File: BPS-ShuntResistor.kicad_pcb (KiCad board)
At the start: 2 copper layers, 40.1 x 35.1 mm, 11 parts, among them J3 Amp_Conn

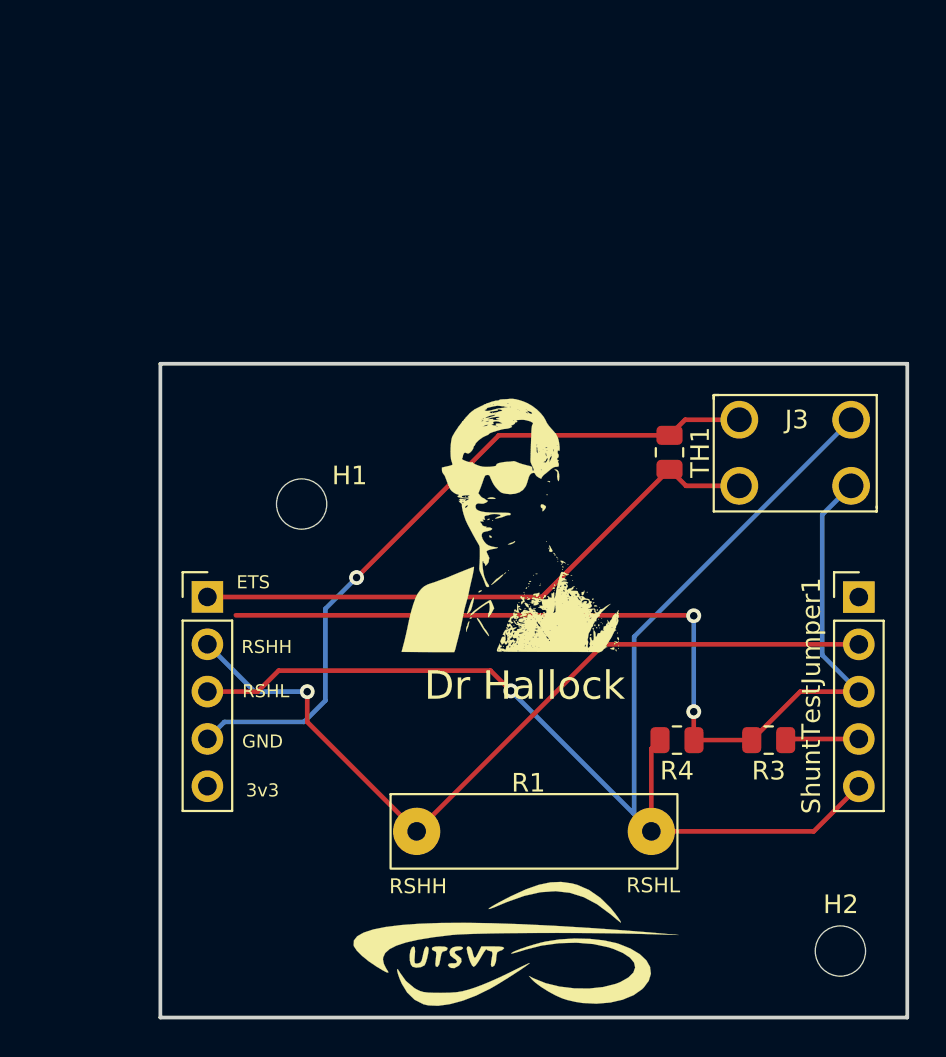
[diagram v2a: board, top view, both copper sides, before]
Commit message: rounding corners, making board a bit smaller
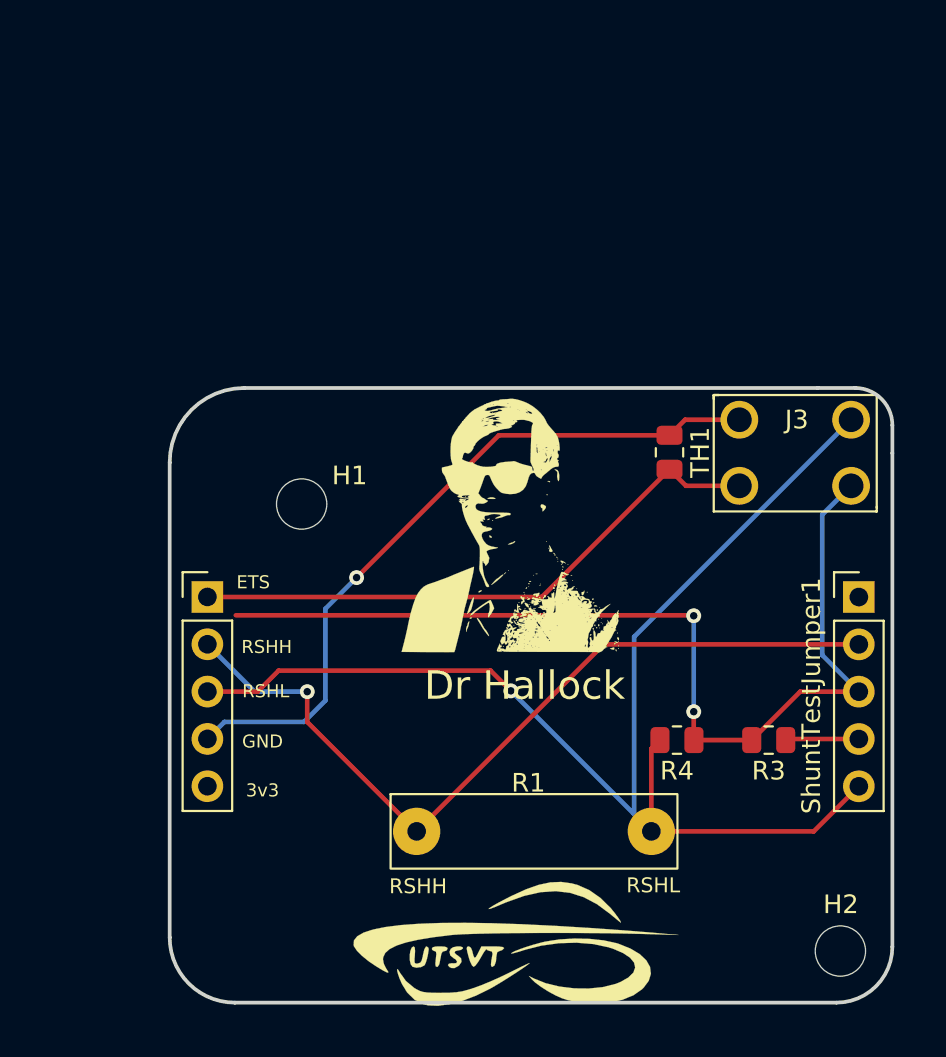
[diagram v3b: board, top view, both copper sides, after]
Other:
- board size 40.1 x 35.1 mm -> 38.8 x 33 mm
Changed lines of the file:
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@@
       (net 3 "RSHL") (pintype "passive"))
   )
-  (gr_rect (start 115 94.9) (end 155.1 130) (layer "Edge.Cuts") (width 0.2) (fill none))
+  (gr_line (start 154.3 126.2) (end 154.300469 99.69887) (layer "Edge.Cuts") (width 0.2))
+  (gr_line (start 119 129.2) (end 151.3 129.2) (layer "Edge.Cuts") (width 0.2))
+  (gr_line (start 154.3 98.2) (end 154.300469 99.69887) (layer "Edge.Cuts") (width 0.2))
+  (gr_line (start 115.5 100.2) (end 115.5 125.7) (layer "Edge.Cuts") (width 0.2))
+  (gr_arc (start 119 129.2) (mid 116.525126 128.174874) (end 115.5 125.7) (layer "Edge.Cuts") (width 0.2))
+  (gr_line (start 152.3 96.2) (end 150.3 96.2) (layer "Edge.Cuts") (width 0.2))
+  (gr_arc (start 115.5 100.2) (mid 116.671573 97.371573) (end 119.5 96.2) (layer "Edge.Cuts") (width 0.2))
+  (gr_arc (start 154.3 126.2) (mid 153.42132 128.32132) (end 151.3 129.2) (layer "Edge.Cuts") (width 0.2))
+  (gr_arc (start 152.3 96.2) (mid 153.714214 96.785786) (end 154.3 98.2) (layer "Edge.Cuts") (width 0.2))
+  (gr_line (start 150.3 96.2) (end 119.5 96.2) (layer "Edge.Cuts") (width 0.2))
   (gr_text "RSHL" (at 141.46 122.905) (layer "F.SilkS")
     (effects (font (size 0.8 0.8) (thickness 0.2)))
@@
     (effects (font (size 1.5 1.5) (thickness 0.3)))
   )
-  (dimension (type aligned) (layer "Cmts.User")
-    (pts (xy 155.075 94.32) (xy 114.975 94.32))
-    (height 4.87)
-    (gr_text "40.1000 mm" (at 135.025 87.65) (layer "Cmts.User")
-      (effects (font (size 1.5 1.5) (thickness 0.3)))
-    )
-    (format (units 3) (units_format 1) (precision 4))
-    (style (thickness 0.2) (arrow_length 1.27) (text_position_mode 0) (extension_height 0.58642) (extension_offset 0.5) keep_text_aligned)
-  )
-  (dimension (type aligned) (layer "Cmts.User")
-    (pts (xy 114.265 94.9) (xy 114.265 130))
-    (height 3.49)
-    (gr_text "35.1000 mm" (at 108.975 112.45 90) (layer "Cmts.User")
-      (effects (font (size 1.5 1.5) (thickness 0.3)))
-    )
-    (format (units 3) (units_format 1) (precision 4))
-    (style (thickness 0.2) (arrow_length 1.27) (text_position_mode 0) (extension_height 0.58642) (extension_offset 0.5) keep_text_aligned)
-  )
-  (dimension (type aligned) (layer "Cmts.User")
-    (pts (xy 151.51 126.405) (xy 151.51 130.005))
-    (height -3.6)
-    (gr_text "3.6000 mm" (at 156.585 128.105 90) (layer "Cmts.User")
-      (effects (font (size 0.5 0.5) (thickness 0.3)))
-    )
-    (format (units 3) (units_format 1) (precision 4))
-    (style (thickness 0.2) (arrow_length 1.27) (text_position_mode 2) (extension_height 0.58642) (extension_offset 0.5) keep_text_aligned)
-  )
-  (dimension (type aligned) (layer "Cmts.User")
-    (pts (xy 122.585 102.43) (xy 122.585 94.83))
-    (height -7.625)
-    (gr_text "7.6000 mm" (at 114.335 98.63 90) (layer "Cmts.User")
-      (effects (font (size 0.5 0.5) (thickness 0.3)))
-    )
-    (format (units 3) (units_format 1) (precision 4))
-    (style (thickness 0.2) (arrow_length 1.27) (text_position_mode 0) (extension_height 0.58642) (extension_offset 0.5) keep_text_aligned)
-  )
-  (dimension (type aligned) (layer "Cmts.User")
-    (pts (xy 154.625 97.925) (xy 154.625 94.925))
-    (height 4.225)
-    (gr_text "3.0000 mm" (at 160.25 96.5 90) (layer "Cmts.User")
-      (effects (font (size 0.6 0.6) (thickness 0.3)))
-    )
-    (format (units 3) (units_format 1) (precision 4))
-    (style (thickness 0.2) (arrow_length 1.27) (text_position_mode 2) (extension_height 0.58642) (extension_offset 0.5) keep_text_aligned)
-  )
-  (dimension (type aligned) (layer "Cmts.User")
-    (pts (xy 128.76 120.005) (xy 128.76 130.005))
-    (height 13.85)
-    (gr_text "10.0000 mm" (at 114.16 125.005 90) (layer "Cmts.User")
-      (effects (font (size 0.6 0.6) (thickness 0.3)))
-    )
-    (format (units 3) (units_format 1) (precision 4))
-    (style (thickness 0.2) (arrow_length 1.27) (text_position_mode 0) (extension_height 0.58642) (extension_offset 0.5) keep_text_aligned)
-  )
-  (dimension (type aligned) (layer "Cmts.User")
-    (pts (xy 128.76 120.005) (xy 115.01 120.005))
-    (height -10.025)
-    (gr_text "13.7500 mm" (at 121.735 130.93) (layer "Cmts.User")
-      (effects (font (size 0.6 0.6) (thickness 0.3)))
-    )
-    (format (units 3) (units_format 1) (precision 4))
-    (style (thickness 0.2) (arrow_length 1.27) (text_position_mode 2) (extension_height 0.58642) (extension_offset 0.5) keep_text_aligned)
-  )
-  (dimension (type aligned) (layer "Cmts.User")
-    (pts (xy 151.51 126.405) (xy 155.11 126.405))
-    (height 3.65)
-    (gr_text "3.6000 mm" (at 153.41 131.38) (layer "Cmts.User")
-      (effects (font (size 0.5 0.5) (thickness 0.3)))
-    )
-    (format (units 3) (units_format 1) (precision 4))
-    (style (thickness 0.2) (arrow_length 1.27) (text_position_mode 2) (extension_height 0.58642) (extension_offset 0.5) keep_text_aligned)
-  )
-  (dimension (type aligned) (layer "Cmts.User")
-    (pts (xy 122.585 102.505) (xy 114.985 102.505))
-    (height 7.675)
-    (gr_text "7.6000 mm" (at 118.785 94.205) (layer "Cmts.User")
-      (effects (font (size 0.5 0.5) (thickness 0.3)))
-    )
-    (format (units 3) (units_format 1) (precision 4))
-    (style (thickness 0.2) (arrow_length 1.27) (text_position_mode 0) (extension_height 0.58642) (extension_offset 0.5) keep_text_aligned)
-  )
-  (dimension (type aligned) (layer "Cmts.User")
-    (pts (xy 152.085 97.905) (xy 155.085 97.905))
-    (height -3.35)
-    (gr_text "3.0000 mm" (at 153.51 93.38) (layer "Cmts.User")
-      (effects (font (size 0.6 0.6) (thickness 0.3)))
-    )
-    (format (units 3) (units_format 1) (precision 4))
-    (style (thickness 0.2) (arrow_length 1.27) (text_position_mode 2) (extension_height 0.58642) (extension_offset 0.5) keep_text_aligned)
-  )
   (segment (start 146.085 101.453) (end 143.2205 101.453) (width 0.25) (layer "F.Cu") (net 1))

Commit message: fixing pcb to look nicer
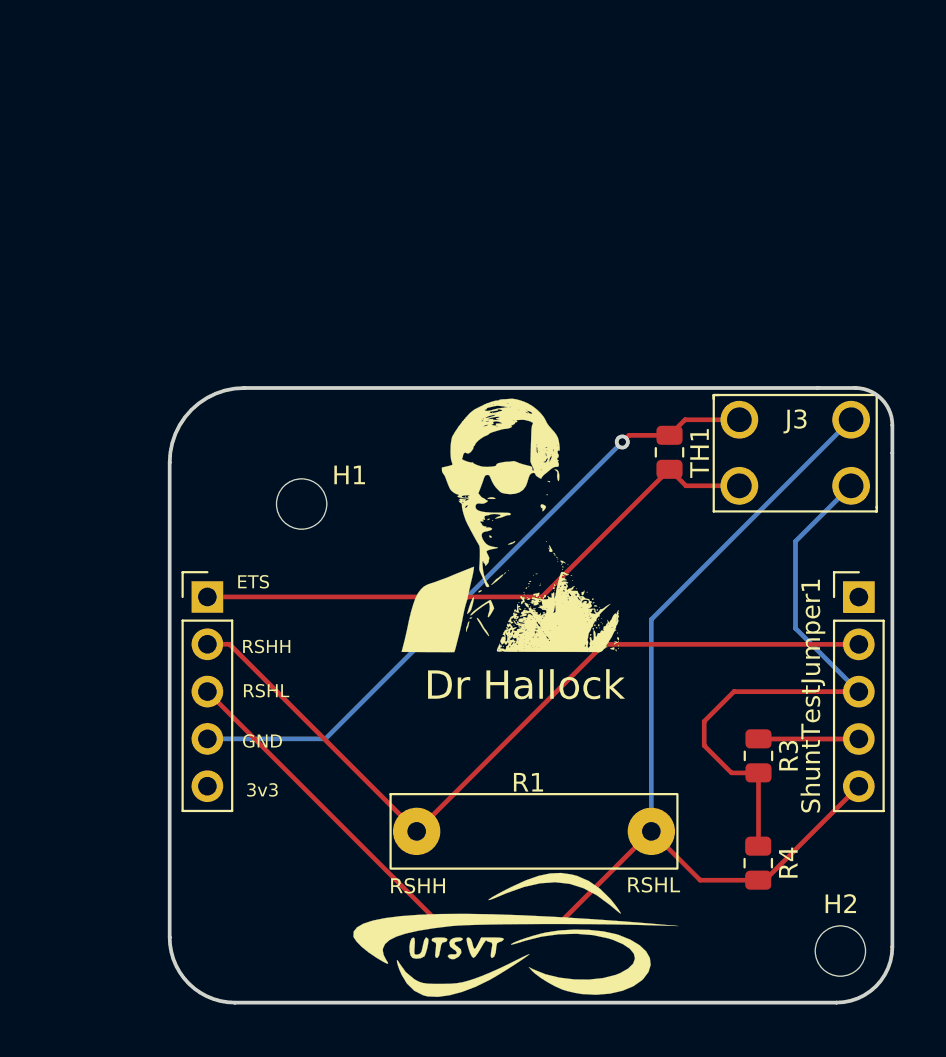
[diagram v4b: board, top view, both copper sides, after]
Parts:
- moved R4 7.92 mm to (147.1, 121.7), turned to -90 degrees
- moved R3 1.01 mm to (147.1, 116.0), turned to -90 degrees
- moved LOGO1 0.48 mm to (133.8, 125.7)
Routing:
- net Net-(J3-Pad2): track 53.7 -> 31.4 mm, vias 2 -> 0
- net GND: track 38.6 -> 35.7 mm
- net /TestIn: track 4.24 -> 5.39 mm
- net RSHH: track 44.2 -> 43.3 mm, vias 1 -> 0
- net RSHL: track 72.4 -> 71.8 mm, vias 1 -> 0

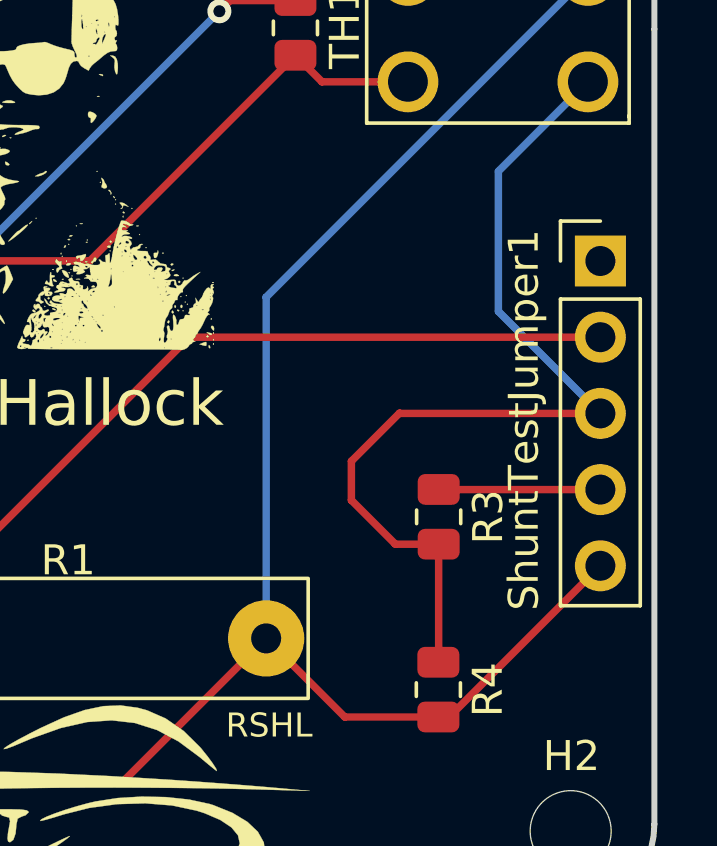
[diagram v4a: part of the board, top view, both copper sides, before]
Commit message: resistor placement change
make tracks more readable + add some text for pins
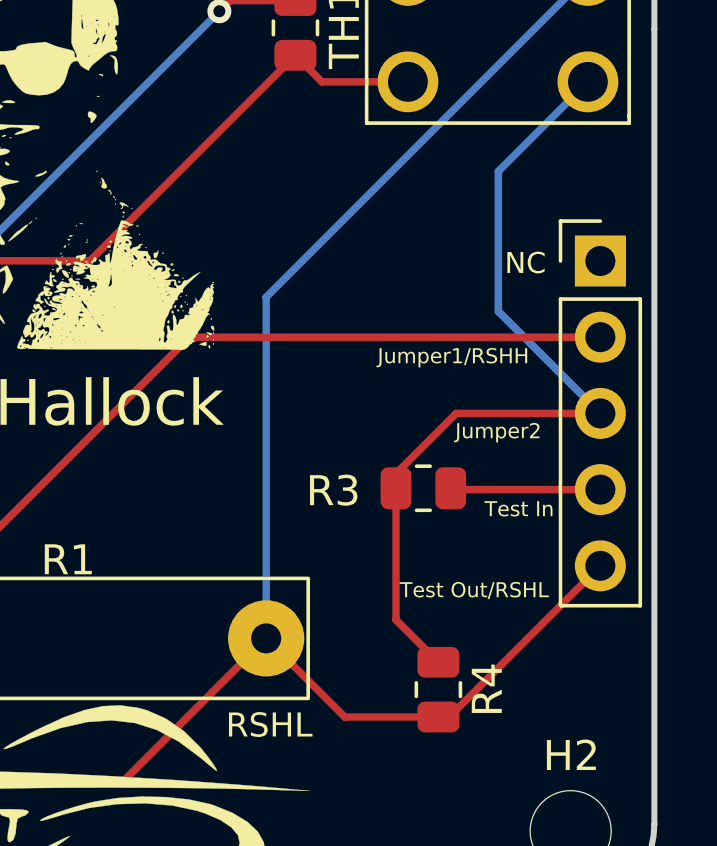
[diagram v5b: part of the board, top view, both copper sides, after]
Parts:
- moved R3 1.08 mm to (146.6, 115.0), turned to 180 degrees
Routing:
- net Net-(J3-Pad2): track 31.4 -> 28.2 mm
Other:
- board text added: "Jumper1/RSHH"
- board text added: "Jumper2"
- board text added: "NC"
- board text added: "Test In"
- board text added: "Test Out/RSHL"
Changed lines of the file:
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@@
   )
   (footprint "Resistor_SMD:R_0805_2012Metric" (layer "F.Cu")
-    (at 147.11 115.9525 -90)
+    (at 146.6 115 180)
     (descr "Resistor SMD 0805 (2012 Metric), square (rectangular) end terminal, IPC_7351 nominal, (Body size source: IPC-SM-782 page 72, https://www.pcb-3d.com/wordpress/wp-content/uploads/ipc-sm-782a_amendment_1_and_2.pdf), generated with kicad-footprint-generator")
     (tags "resistor")
@@
     (property "Sheetname" "")
     (attr smd)
-    (fp_text reference "R3" (at 0 -1.65 -270) (layer "F.SilkS")
+    (fp_text reference "R3" (at 3 -0.1) (layer "F.SilkS")
       (effects (font (size 1 1) (thickness 0.15)))
     )
-    (fp_text value "34k" (at 0 1.65 -270) (layer "F.Fab")
+    (fp_text value "34k" (at 0 1.65) (layer "F.Fab")
       (effects (font (size 1 1) (thickness 0.15)))
     )
-    (fp_text user "${REFERENCE}" (at 0 0 -270) (layer "F.Fab")
+    (fp_text user "${REFERENCE}" (at 0 0) (layer "F.Fab")
       (effects (font (size 0.5 0.5) (thickness 0.08)))
     )
@@
     (fp_line (start 1 0.625) (end -1 0.625) (layer "F.Fab") (width 0.1))
     (fp_line (start -1 0.625) (end -1 -0.625) (layer "F.Fab") (width 0.1))
-    (pad "1" smd roundrect (at -0.9125 0 270) (size 1.025 1.4) (layers "F.Cu" "F.Paste" "F.Mask") (roundrect_rratio 0.243902439)
+    (pad "1" smd roundrect (at -0.9125 0 180) (size 1.025 1.4) (layers "F.Cu" "F.Paste" "F.Mask") (roundrect_rratio 0.243902439)
       (net 6 "/TestIn") (pintype "passive"))
-    (pad "2" smd roundrect (at 0.9125 0 270) (size 1.025 1.4) (layers "F.Cu" "F.Paste" "F.Mask") (roundrect_rratio 0.243902439)
+    (pad "2" smd roundrect (at 0.9125 0 180) (size 1.025 1.4) (layers "F.Cu" "F.Paste" "F.Mask") (roundrect_rratio 0.243902439)
       (net 7 "Net-(J3-Pad2)") (pintype "passive"))
     (model "${KICAD6_3DMODEL_DIR}/Resistor_SMD.3dshapes/R_0805_2012Metric.wrl"
@@
     (property "Sheetname" "")
     (attr through_hole)
-    (fp_text reference "ShuntTestJumper1" (at -2.55 5.3 90) (layer "F.SilkS")
+    (fp_text reference "ShuntTestJumper1" (at -2.55 5.3 90) (layer "F.SilkS") hide
       (effects (font (size 1 1) (thickness 0.15)))
     )
@@
     (effects (font (size 0.7 0.7) (thickness 0.175)))
   )
+  (gr_text "Jumper1/RSHH\n" (at 147.6 110.6) (layer "F.SilkS")
+    (effects (font (size 0.5 0.5) (thickness 0.125)))
+  )
   (gr_text "ETS" (at 119.985 106.63) (layer "F.SilkS")
     (effects (font (size 0.7 0.7) (thickness 0.175)))
@@
     (effects (font (size 0.7 0.7) (thickness 0.175)))
   )
+  (gr_text "Jumper2" (at 149.1 113.1) (layer "F.SilkS")
+    (effects (font (size 0.5 0.5) (thickness 0.125)))
+  )
+  (gr_text "NC\n" (at 150 107.5) (layer "F.SilkS")
+    (effects (font (size 0.7 0.7) (thickness 0.125)))
+  )
   (gr_text "GND" (at 120.485 115.18) (layer "F.SilkS")
     (effects (font (size 0.7 0.7) (thickness 0.175)))
@@
     (effects (font (size 0.8 0.8) (thickness 0.2)))
   )
+  (gr_text "Test In" (at 149.8 115.7) (layer "F.SilkS")
+    (effects (font (size 0.5 0.5) (thickness 0.125)))
+  )
+  (gr_text "Test Out/RSHL" (at 148.3 118.4) (layer "F.SilkS")
+    (effects (font (size 0.5 0.5) (thickness 0.125)))
+  )
   (gr_text "RSHH" (at 120.71 110.105) (layer "F.SilkS")
     (effects (font (size 0.7 0.7) (thickness 0.175)))
@@
   (segment (start 123.86 115.04) (end 117.525 115.04) (width 0.25) (layer "B.Cu") (net 4))
   (segment (start 139.8 99.1) (end 123.86 115.04) (width 0.25) (layer "B.Cu") (net 4))
-  (segment (start 147.11 115.04) (end 147.115 115.045) (width 0.25) (layer "F.Cu") (net 6))
-  (segment (start 147.115 115.045) (end 152.5 115.045) (width 0.25) (layer "F.Cu") (net 6))
-  (segment (start 144.2 114.1) (end 145.8 112.5) (width 0.25) (layer "F.Cu") (net 7))
-  (segment (start 145.8 112.5) (end 145.805 112.505) (width 0.25) (layer "F.Cu") (net 7))
+  (segment (start 147.5125 115) (end 147.5575 115.045) (width 0.25) (layer "F.Cu") (net 6))
+  (segment (start 147.5575 115.045) (end 152.5 115.045) (width 0.25) (layer "F.Cu") (net 6))
+  (segment (start 147.1 120.8) (end 145.6875 119.3875) (width 0.25) (layer "F.Cu") (net 7))
   (segment (start 147.11 120.79) (end 147.1 120.8) (width 0.25) (layer "F.Cu") (net 7))
-  (segment (start 147.11 116.865) (end 145.665 116.865) (width 0.25) (layer "F.Cu") (net 7))
-  (segment (start 147.11 116.865) (end 147.11 120.79) (width 0.25) (layer "F.Cu") (net 7))
-  (segment (start 145.665 116.865) (end 144.2 115.4) (width 0.25) (layer "F.Cu") (net 7))
-  (segment (start 145.805 112.505) (end 152.5 112.505) (width 0.25) (layer "F.Cu") (net 7))
-  (segment (start 144.2 115.4) (end 144.2 114.1) (width 0.25) (layer "F.Cu") (net 7))
+  (segment (start 145.6875 119.3875) (end 145.6875 115) (width 0.25) (layer "F.Cu") (net 7))
+  (segment (start 145.6875 114.5125) (end 147.695 112.505) (width 0.25) (layer "F.Cu") (net 7))
+  (segment (start 147.695 112.505) (end 152.5 112.505) (width 0.25) (layer "F.Cu") (net 7))
+  (segment (start 145.6875 115) (end 145.6875 114.5125) (width 0.25) (layer "F.Cu") (net 7))
   (segment (start 149.1 109.105) (end 152.5 112.505) (width 0.25) (layer "B.Cu") (net 7))
   (segment (start 149.1 104.438) (end 149.1 109.105) (width 0.25) (layer "B.Cu") (net 7))
